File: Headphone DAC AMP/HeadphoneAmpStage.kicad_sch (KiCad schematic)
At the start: 19 parts, among them U3 TPA6120A2DWP, U4 OPA1612AxD, U5 OPA1612AxD

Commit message: Power updated
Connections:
- net ROUT is gone; now on an unnamed net: R10.2
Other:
- moved on the sheet: R10, R9

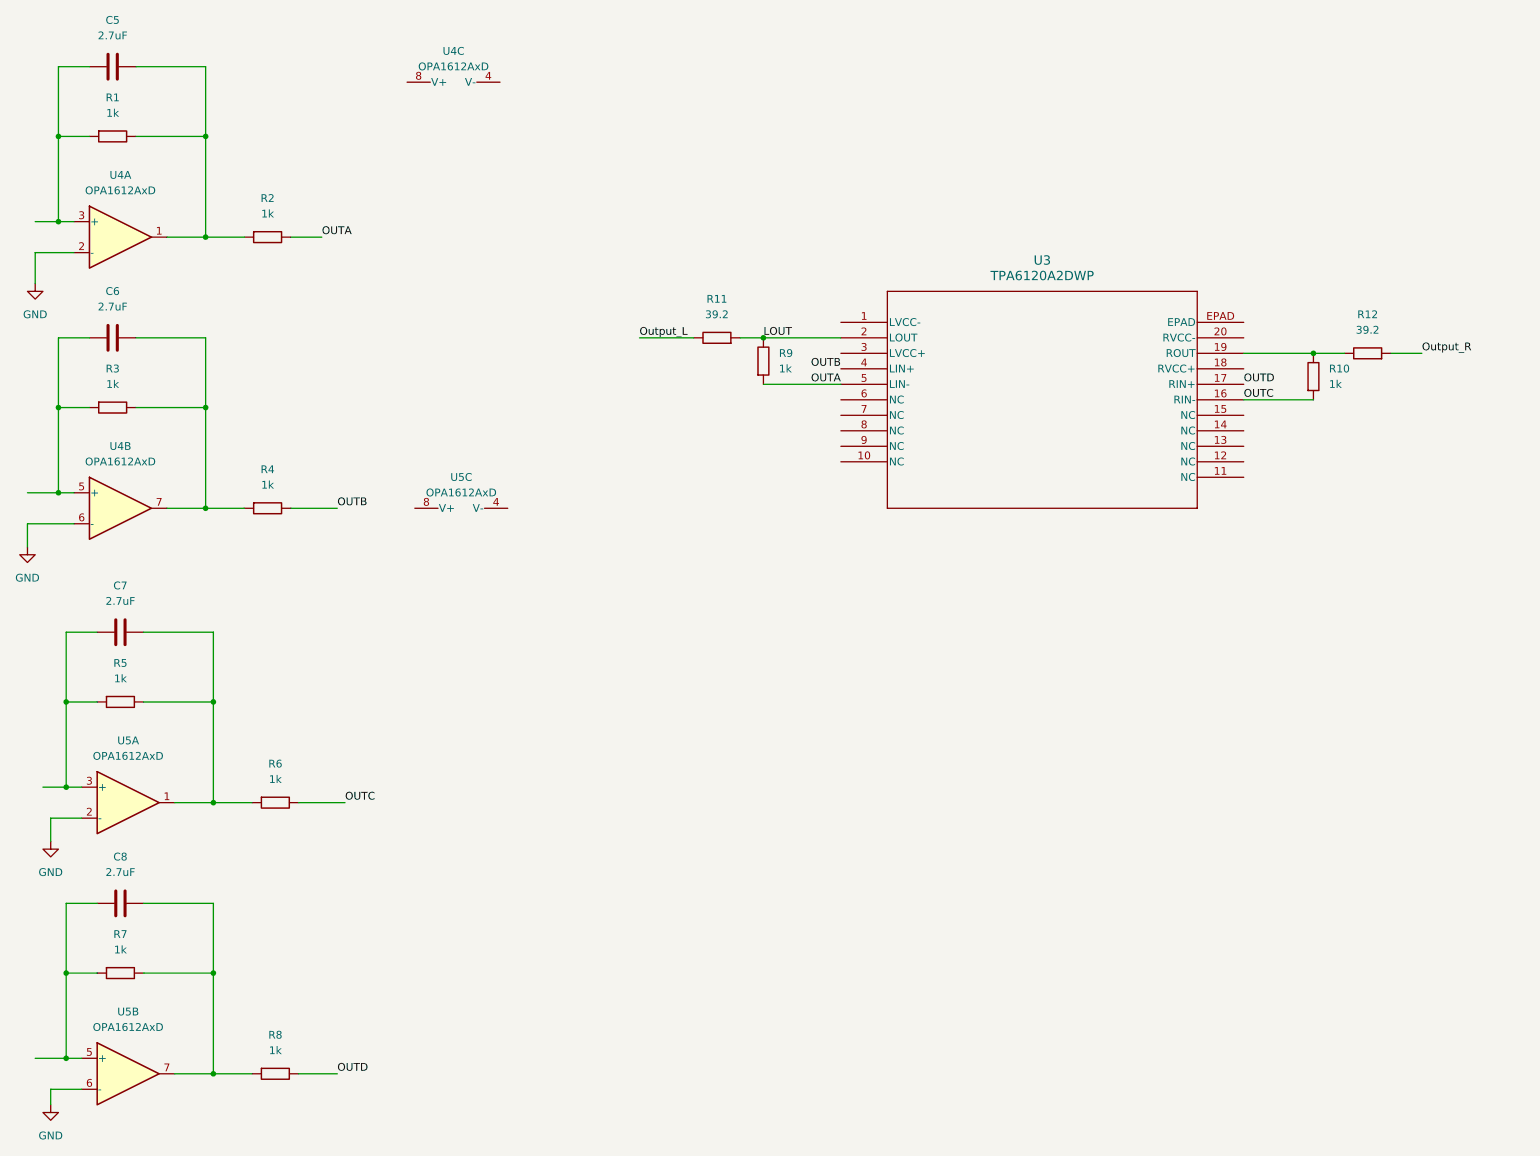
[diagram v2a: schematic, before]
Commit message: Finished AMP Stage
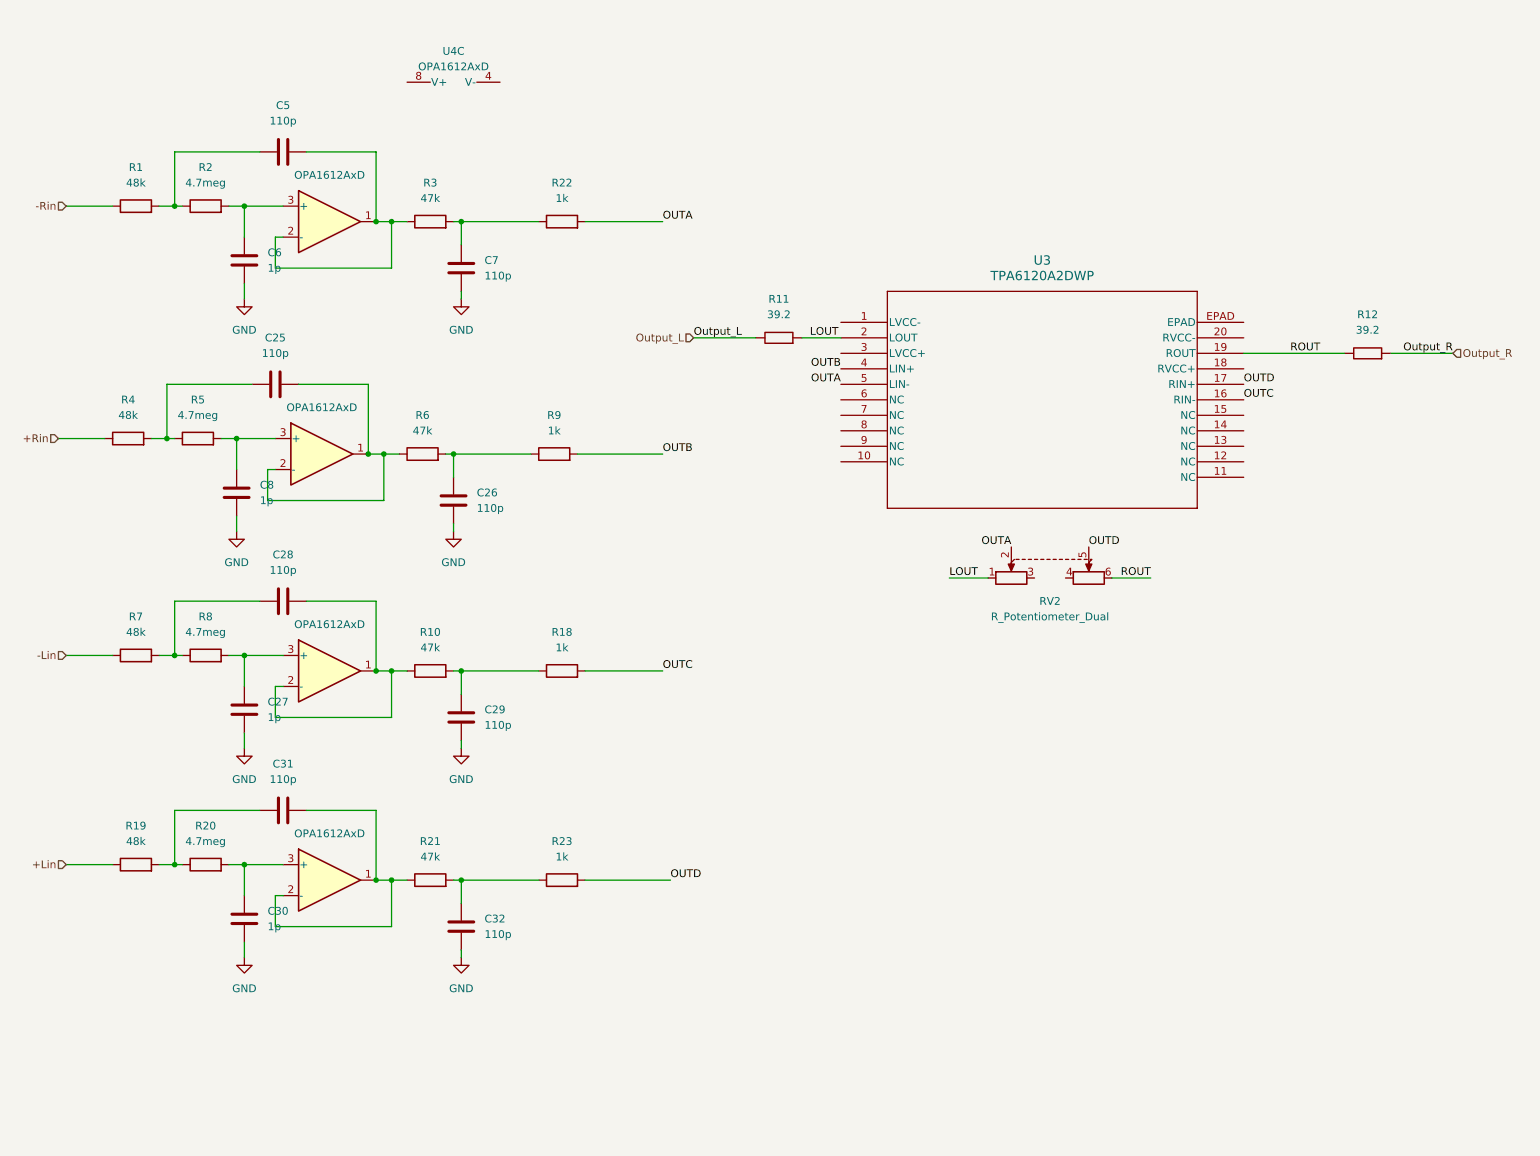
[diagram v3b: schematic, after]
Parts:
- removed R1, R10, R2, R3, R4, R5, R6, R7, R8, R9: 1k, Resistor_THT:R_Axial_DIN0207_L6.3mm_D2.5mm_P10.16mm_Horizontal, symbol PCM_SL_Resistors:Resistor
- removed unit 2 of U4
- removed unit 2 of U5
- removed unit 3 of U5
- added C25, C26, C28, C29, C31, C32: 110p, symbol Device:C
- added C27, C30: 1p, symbol Device:C
- added R1, R19, R4, R7: 48k, symbol Device:R
- added R10, R21, R3, R6: 47k, symbol Device:R
- added R18, R22, R23, R9: 1k, symbol Device:R
- added R2, R20, R5, R8: 4.7meg, symbol Device:R
- added RV2: R_Potentiometer_Dual, symbol Device:R_Potentiometer_Dual
- added U12, U13: OPA1612AxD, symbol Amplifier_Operational:OPA1612AxD
- C5, C7: value 2.7uF -> 110p
- C6, C8: value 2.7uF -> 1p
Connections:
- net GND: now also C6.2, C7.2, C8.2, C26.2, C27.2, C29.2, C30.2, C32.2; no longer U4.2 (-), U5.2 (-)
- net LOUT: now also RV2.1
- net OUTA: now also R22.2, RV2.2
- net OUTB: now also R9.2
- net OUTC: now also R18.2
- net OUTD: now also R23.2, RV2.5
- net at U4.3 (+): now also C6.1, R2.2; no longer C5.2
- net at U4.1: now also C5.2, U4.2 (-), R3.1; no longer C5.1
- net at C7.1: now also R22.1, R3.2; no longer U5.1
- net at U5.3 (+): now also C8.1, R5.2; no longer C7.2
- net ROUT: now reaches R12.2, U3.19 (ROUT)
- net ROUT: now also RV2.6
- new net: C31.1, R19.2, R20.1
- new net: C29.1, R10.2, R18.1
- new net: C30.1, R20.2, U13.3 (+)
- new net: C27.1, R8.2, U12.3 (+)
- new net: C25.1, R4.2, R5.1
- new net: C26.1, R6.2, R9.1
- new net: C25.2, R6.1, U5.1, U5.2 (-)
- new net: C28.1, R7.2, R8.1
- new net: C28.2, R10.1, U12.1, U12.2 (-)
- new net: C31.2, R21.1, U13.1, U13.2 (-)
- new net: C32.1, R21.2, R23.1
- new net: C5.1, R1.2, R2.1
- new net +Lin: R19.1
- new net +Rin: R4.1
- new net -Lin: R7.1
- new net -Rin: R1.1
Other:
- moved on the sheet: R11

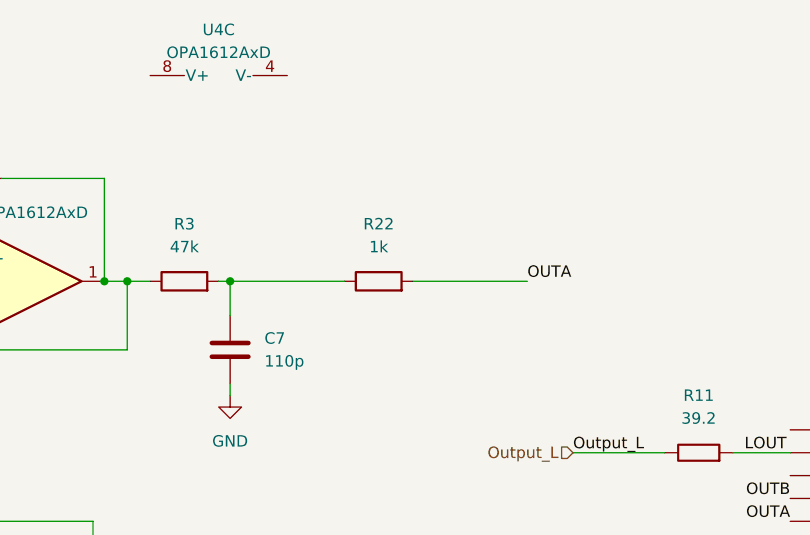
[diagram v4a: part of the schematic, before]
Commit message: LDO Low Noise Rails 3.3 and 1.8
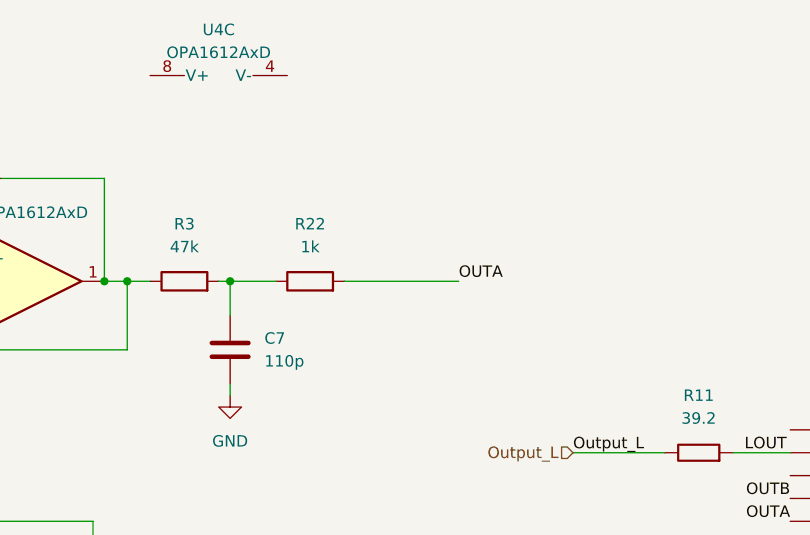
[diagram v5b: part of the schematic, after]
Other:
- moved on the sheet: R22
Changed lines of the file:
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@@
 	(wire
 		(pts
-			(xy 107.95 46.99) (xy 120.65 46.99)
+			(xy 100.33 46.99) (xy 113.03 46.99)
 		)
 		(stroke
@@
 	(wire
 		(pts
-			(xy 87.63 46.99) (xy 100.33 46.99)
+			(xy 87.63 46.99) (xy 92.71 46.99)
 		)
 		(stroke
@@
 	)
 	(label "OUTA"
-		(at 120.65 46.99 0)
+		(at 113.03 46.99 0)
 		(effects
 			(font
@@
 	(symbol
 		(lib_id "Device:R")
-		(at 104.14 46.99 90)
+		(at 96.52 46.99 90)
 		(unit 1)
 		(exclude_from_sim no)
@@
 		(fields_autoplaced yes)
 		(property "Reference" "R22"
-			(at 104.14 40.64 90)
+			(at 96.52 40.64 90)
 			(effects
 				(font
@@
 		)
 		(property "Value" "1k"
-			(at 104.14 43.18 90)
+			(at 96.52 43.18 90)
 			(effects
 				(font
@@
 		)
 		(property "Footprint" ""
-			(at 104.14 48.768 90)
+			(at 96.52 48.768 90)
 			(effects
 				(font
@@
 		)
 		(property "Datasheet" "~"
-			(at 104.14 46.99 0)
+			(at 96.52 46.99 0)
 			(effects
 				(font
@@
 		)
 		(property "Description" "Resistor"
-			(at 104.14 46.99 0)
-			(effects
-				(font
+			(at 96.52 46.99 0)
+			(effects
+				(font

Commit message: Completed a significant amount of the power and routing
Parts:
- C25, C26, C27, C28, C29, C30, C31, C32, C5, C6, C7, C8: footprint (none) -> Capacitor_SMD:C_0805_2012Metric_Pad1.18x1.45mm_HandSolder
- R1, R10, R18, R19, R2, R20, R21, R22, R23, R3, R4, R5, R6, R7, R8, R9: footprint (none) -> Resistor_SMD:R_0805_2012Metric_Pad1.20x1.40mm_HandSolder
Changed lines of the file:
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@@
 			)
 		)
-		(property "Footprint" ""
+		(property "Footprint" "Resistor_SMD:R_0805_2012Metric_Pad1.20x1.40mm_HandSolder"
 			(at 34.29 154.178 90)
 			(effects
@@
 			)
 		)
-		(property "Footprint" ""
+		(property "Footprint" "Capacitor_SMD:C_0805_2012Metric_Pad1.18x1.45mm_HandSolder"
 			(at 88.5952 132.08 0)
 			(effects
@@
 			)
 		)
-		(property "Footprint" ""
+		(property "Footprint" "Resistor_SMD:R_0805_2012Metric_Pad1.20x1.40mm_HandSolder"
 			(at 45.72 154.178 90)
 			(effects
@@
 			)
 		)
-		(property "Footprint" ""
+		(property "Footprint" "Capacitor_SMD:C_0805_2012Metric_Pad1.18x1.45mm_HandSolder"
 			(at 53.0352 130.81 0)
 			(effects
@@
 			)
 		)
-		(property "Footprint" ""
+		(property "Footprint" "Resistor_SMD:R_0805_2012Metric_Pad1.20x1.40mm_HandSolder"
 			(at 44.45 84.328 90)
 			(effects
@@
 			)
 		)
-		(property "Footprint" ""
+		(property "Footprint" "Resistor_SMD:R_0805_2012Metric_Pad1.20x1.40mm_HandSolder"
 			(at 96.52 48.768 90)
 			(effects
@@
 			)
 		)
-		(property "Footprint" ""
+		(property "Footprint" "Capacitor_SMD:C_0805_2012Metric_Pad1.18x1.45mm_HandSolder"
 			(at 53.0352 57.15 0)
 			(effects
@@
 			)
 		)
-		(property "Footprint" ""
+		(property "Footprint" "Capacitor_SMD:C_0805_2012Metric_Pad1.18x1.45mm_HandSolder"
 			(at 87.3252 96.52 0)
 			(effects
@@
 			)
 		)
-		(property "Footprint" ""
+		(property "Footprint" "Capacitor_SMD:C_0805_2012Metric_Pad1.18x1.45mm_HandSolder"
 			(at 60.96 72.6948 0)
 			(effects
@@
 			)
 		)
-		(property "Footprint" ""
+		(property "Footprint" "Capacitor_SMD:C_0805_2012Metric_Pad1.18x1.45mm_HandSolder"
 			(at 62.23 108.2548 0)
 			(effects
@@
 			)
 		)
-		(property "Footprint" ""
+		(property "Footprint" "Capacitor_SMD:C_0805_2012Metric_Pad1.18x1.45mm_HandSolder"
 			(at 88.5952 58.42 0)
 			(effects
@@
 			)
 		)
-		(property "Footprint" ""
+		(property "Footprint" "Resistor_SMD:R_0805_2012Metric_Pad1.20x1.40mm_HandSolder"
 			(at 82.55 156.718 90)
 			(effects
@@
 			)
 		)
-		(property "Footprint" ""
+		(property "Footprint" "Resistor_SMD:R_0805_2012Metric_Pad1.20x1.40mm_HandSolder"
 			(at 104.14 156.718 90)
 			(effects
@@
 			)
 		)
-		(property "Footprint" ""
+		(property "Footprint" "Resistor_SMD:R_0805_2012Metric_Pad1.20x1.40mm_HandSolder"
 			(at 33.02 84.328 90)
 			(effects
@@
 			)
 		)
-		(property "Footprint" ""
+		(property "Footprint" "Capacitor_SMD:C_0805_2012Metric_Pad1.18x1.45mm_HandSolder"
 			(at 62.23 34.5948 0)
 			(effects
@@
 			)
 		)
-		(property "Footprint" ""
+		(property "Footprint" "Resistor_SMD:R_0805_2012Metric_Pad1.20x1.40mm_HandSolder"
 			(at 34.29 46.228 90)
 			(effects
@@
 			)
 		)
-		(property "Footprint" ""
+		(property "Footprint" "Resistor_SMD:R_0805_2012Metric_Pad1.20x1.40mm_HandSolder"
 			(at 81.28 86.868 90)
 			(effects
@@
 			)
 		)
-		(property "Footprint" ""
+		(property "Footprint" "Resistor_SMD:R_0805_2012Metric_Pad1.20x1.40mm_HandSolder"
 			(at 45.72 119.888 90)
 			(effects
@@
 			)
 		)
-		(property "Footprint" ""
+		(property "Footprint" "Resistor_SMD:R_0805_2012Metric_Pad1.20x1.40mm_HandSolder"
 			(at 104.14 122.428 90)
 			(effects
@@
 			)
 		)
-		(property "Footprint" ""
+		(property "Footprint" "Capacitor_SMD:C_0805_2012Metric_Pad1.18x1.45mm_HandSolder"
 			(at 53.0352 165.1 0)
 			(effects
@@
 			)
 		)
-		(property "Footprint" ""
+		(property "Footprint" "Resistor_SMD:R_0805_2012Metric_Pad1.20x1.40mm_HandSolder"
 			(at 102.87 86.868 90)
 			(effects
@@
 			)
 		)
-		(property "Footprint" ""
+		(property "Footprint" "Resistor_SMD:R_0805_2012Metric_Pad1.20x1.40mm_HandSolder"
 			(at 82.55 48.768 90)
 			(effects
@@
 			)
 		)
-		(property "Footprint" ""
+		(property "Footprint" "Resistor_SMD:R_0805_2012Metric_Pad1.20x1.40mm_HandSolder"
 			(at 82.55 122.428 90)
 			(effects
@@
 			)
 		)
-		(property "Footprint" ""
+		(property "Footprint" "Capacitor_SMD:C_0805_2012Metric_Pad1.18x1.45mm_HandSolder"
 			(at 62.23 142.5448 0)
 			(effects
@@
 			)
 		)
-		(property "Footprint" ""
+		(property "Footprint" "Capacitor_SMD:C_0805_2012Metric_Pad1.18x1.45mm_HandSolder"
 			(at 88.5952 166.37 0)
 			(effects
@@
 			)
 		)
-		(property "Footprint" ""
+		(property "Footprint" "Resistor_SMD:R_0805_2012Metric_Pad1.20x1.40mm_HandSolder"
 			(at 34.29 119.888 90)
 			(effects
@@
 			)
 		)
-		(property "Footprint" ""
+		(property "Footprint" "Resistor_SMD:R_0805_2012Metric_Pad1.20x1.40mm_HandSolder"
 			(at 45.72 46.228 90)
 			(effects
@@
 			)
 		)
-		(property "Footprint" ""
+		(property "Footprint" "Capacitor_SMD:C_0805_2012Metric_Pad1.18x1.45mm_HandSolder"
 			(at 51.7652 95.25 0)
 			(effects

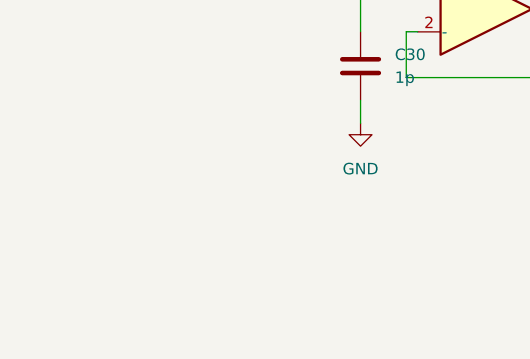
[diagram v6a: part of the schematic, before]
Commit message: Added ground and 0.9v
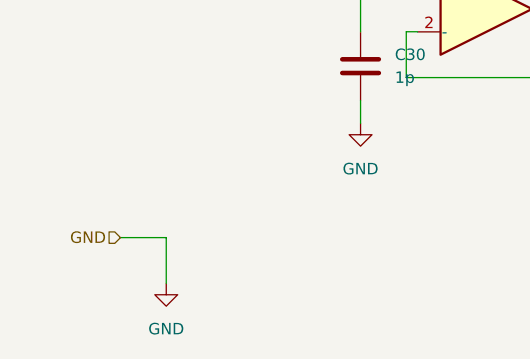
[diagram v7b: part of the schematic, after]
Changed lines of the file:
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@@
 	(wire
 		(pts
+			(xy 30.48 180.34) (xy 30.48 185.42)
+		)
+		(stroke
+			(width 0)
+			(type default)
+		)
+	)
+	(wire
+		(pts
 			(xy 87.63 124.46) (xy 87.63 120.65)
 		)
@@
 	(wire
 		(pts
+			(xy 25.4 180.34) (xy 30.48 180.34)
+		)
+		(stroke
+			(width 0)
+			(type default)
+		)
+	)
+	(wire
+		(pts
 			(xy 57.15 157.48) (xy 58.42 157.48)
 		)
@@
 		)
 	)
+	(hierarchical_label "GND"
+		(shape input)
+		(at 25.4 180.34 180)
+		(effects
+			(font
+				(size 1.27 1.27)
+			)
+			(justify right)
+		)
+	)
 	(hierarchical_label "-Rin"
 		(shape input)
@@
 					(unit 1)
 				)
+			)
+		)
+	)
+	(symbol
+		(lib_id "power:GND")
+		(at 30.48 185.42 0)
+		(unit 1)
+		(exclude_from_sim no)
+		(in_bom yes)
+		(on_board yes)
+		(dnp no)
+		(fields_autoplaced yes)
+		(property "Reference" "#PWR084"
+			(at 30.48 191.77 0)
+			(effects
+				(font
+					(size 1.27 1.27)
+				)
+				(hide yes)
+			)
+		)
+		(property "Value" "GND"
+			(at 30.48 190.5 0)
+			(effects
+				(font
+					(size 1.27 1.27)
+				)
+			)
+		)
+		(property "Footprint" ""
+			(at 30.48 185.42 0)
+			(effects
+				(font
+					(size 1.27 1.27)
+				)
+				(hide yes)
+			)
+		)
+		(property "Datasheet" ""
+			(at 30.48 185.42 0)
+			(effects
+				(font
+					(size 1.27 1.27)
+				)
+				(hide yes)
+			)
+		)
+		(property "Description" "Power symbol creates a global label with name \"GND\" , ground"
+			(at 30.48 185.42 0)
+			(effects
+				(font
+					(size 1.27 1.27)
+				)
+				(hide yes)
+			)
+		)
+		(pin "1"
+		)
+		(instances
+			(project "Headphone DAC AMP"
+				(path "/d034eddd-efbc-47be-a25c-37cbfbab4cd8/a8d45096-939e-42db-8984-b3f2d55a20c4"
+					(reference "#PWR084")
+					(unit 1)
+				)
